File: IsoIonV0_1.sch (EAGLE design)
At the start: 52 parts, among them IC1 MCP3221, IC2 MCP4017-100K, IC4 TL072, IC5 TPS60400DBV

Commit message: Cleaned up sch small silkscreen adjustment on brd
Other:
- note added: "ADC and vRef"
- note added: "I2C Isolation"
- note added: "Isolated DC-DC"
- note added: "Mechanical Section"
- note added: "Reverse Voltage Protection"
- note added: "Standard header"
- note removed: "12 bit ADC"
- moved on the sheet: C1, C10, C11, C12, C13, C14, C15, C2, C3, C5, C6, C7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

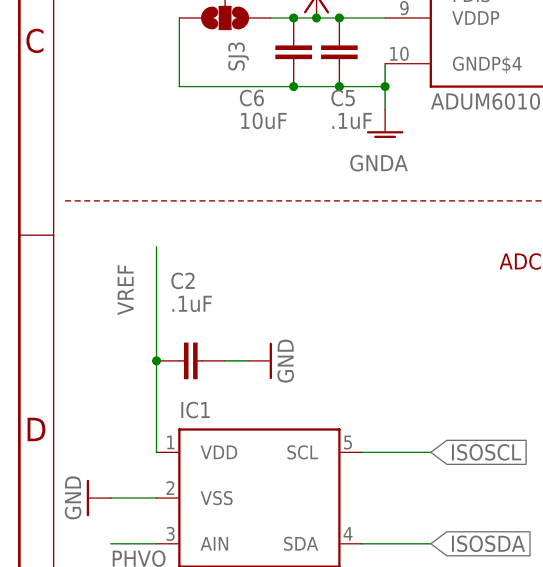
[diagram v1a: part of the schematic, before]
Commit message: MCP4017 package updated to SC70-6
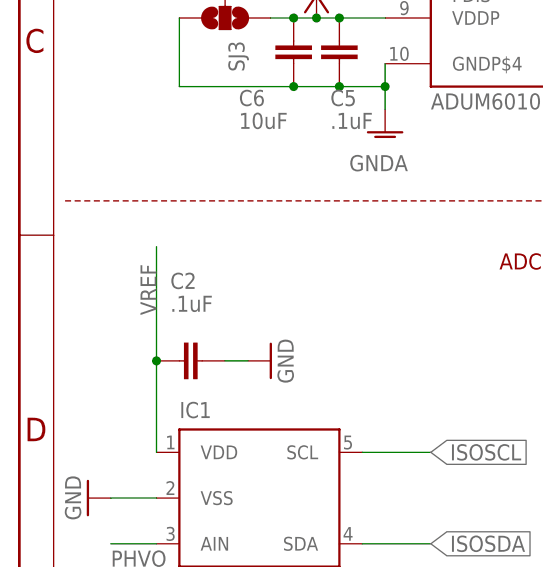
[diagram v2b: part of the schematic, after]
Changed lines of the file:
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@@
 <pinref part="C2" gate="G$1" pin="2"/>
 <wire x1="15.24" y1="33.02" x2="15.24" y2="45.72" width="0.1524" layer="91"/>
-<label x="12.7" y="38.1" size="1.778" layer="95" rot="R90"/>
+<label x="15.24" y="38.1" size="1.778" layer="95" rot="R90"/>
 <pinref part="IC1" gate="G$1" pin="VDD"/>
 <wire x1="15.24" y1="33.02" x2="15.24" y2="22.86" width="0.1524" layer="91"/>

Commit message: Routed Offset from VREF instead of VDD
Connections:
- net VDD: no longer R12.1
- net VREF: now also R12.1
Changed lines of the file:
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@@
 <junction x="15.24" y="33.02"/>
+</segment>
+<segment>
+<pinref part="R12" gate="G$1" pin="1"/>
+<wire x1="187.96" y1="119.38" x2="190.5" y2="119.38" width="0.1524" layer="91"/>
+<label x="187.96" y="119.38" size="1.778" layer="95" rot="R180" xref="yes"/>
 </segment>
 </net>
@@
 <pinref part="IC4" gate="P" pin="V+"/>
 <pinref part="VDD6" gate="G$1" pin="VDD"/>
-<wire x1="187.96" y1="119.38" x2="190.5" y2="119.38" width="0.1524" layer="91"/>
-<pinref part="R12" gate="G$1" pin="1"/>
-<wire x1="187.96" y1="119.38" x2="187.96" y2="109.22" width="0.1524" layer="91"/>
-<wire x1="187.96" y1="109.22" x2="182.88" y2="109.22" width="0.1524" layer="91"/>
-<junction x="182.88" y="109.22"/>
 </segment>
 </net>

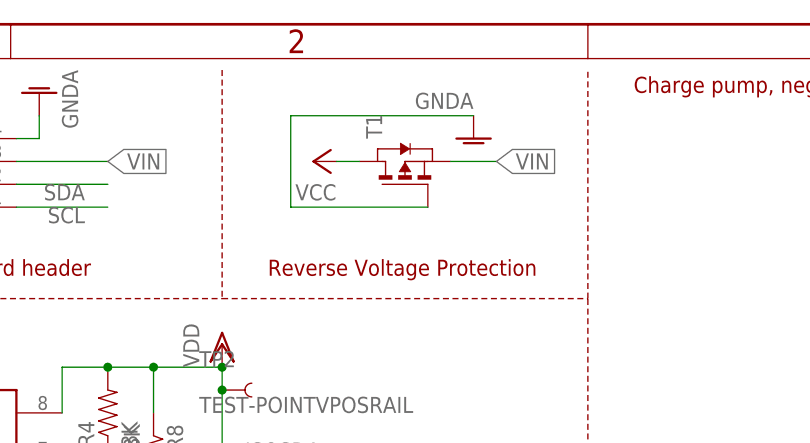
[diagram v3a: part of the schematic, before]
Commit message: Flip pins on PMos reverse protection FET
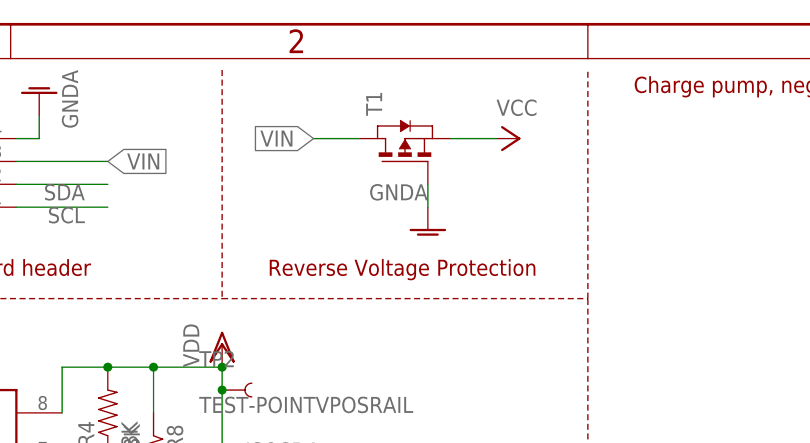
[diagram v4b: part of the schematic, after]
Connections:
- net VCC: now also T1.S; no longer T1.D
- net VIN: now also T1.D; no longer T1.S
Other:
- moved on the sheet: T1
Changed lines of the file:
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@@
 <attribute name="VALUE" x="166.624" y="168.021" size="1.778" layer="96"/>
 </instance>
-<instance part="T1" gate="A" x="111.76" y="165.1" rot="R90"/>
-<instance part="GND21" gate="1" x="119.38" y="167.64" smashed="yes">
-<attribute name="VALUE" x="119.38" y="172.72" size="1.778" layer="96" rot="R180"/>
+<instance part="T1" gate="A" x="111.76" y="167.64" rot="R90"/>
+<instance part="GND21" gate="1" x="114.3" y="157.48" smashed="yes">
+<attribute name="VALUE" x="114.3" y="162.56" size="1.778" layer="96" rot="R180"/>
 </instance>
 <instance part="U$3" gate="G$1" x="220.98" y="10.16"/>
-<instance part="P+1" gate="VCC" x="101.6" y="165.1" rot="R90"/>
+<instance part="P+1" gate="VCC" x="124.46" y="167.64" rot="R270"/>
 <instance part="TP1" gate="G$1" x="81.28" y="121.92" smashed="yes" rot="R270">
 <attribute name="NAME" x="83.82" y="124.46" size="1.778" layer="95" rot="R270"/>
@@
 </segment>
 <segment>
-<wire x1="119.38" y1="170.18" x2="99.06" y2="170.18" width="0.1524" layer="91"/>
-<wire x1="99.06" y1="170.18" x2="99.06" y2="160.02" width="0.1524" layer="91"/>
-<wire x1="99.06" y1="160.02" x2="114.3" y2="160.02" width="0.1524" layer="91"/>
 <pinref part="T1" gate="A" pin="G"/>
+<wire x1="114.3" y1="162.56" x2="114.3" y2="160.02" width="0.1524" layer="91"/>
 <pinref part="GND21" gate="1" pin="GNDA"/>
 </segment>
@@
 </segment>
 <segment>
-<wire x1="104.14" y1="165.1" x2="106.68" y2="165.1" width="0.1524" layer="91"/>
-<pinref part="T1" gate="A" pin="D"/>
+<pinref part="T1" gate="A" pin="S"/>
 <pinref part="P+1" gate="VCC" pin="VCC"/>
+<wire x1="116.84" y1="167.64" x2="121.92" y2="167.64" width="0.1524" layer="91"/>
 </segment>
 </net>
@@
 </segment>
 <segment>
-<pinref part="T1" gate="A" pin="S"/>
-<wire x1="116.84" y1="165.1" x2="121.92" y2="165.1" width="0.1524" layer="91"/>
-<label x="121.92" y="165.1" size="1.778" layer="95" xref="yes"/>
-</segment>
-</net>
+<pinref part="T1" gate="A" pin="D"/>
+<wire x1="106.68" y1="167.64" x2="101.6" y2="167.64" width="0.1524" layer="91"/>
+<label x="101.6" y="167.64" size="1.778" layer="95" rot="R180" xref="yes"/>
+</segment>
+</net>
